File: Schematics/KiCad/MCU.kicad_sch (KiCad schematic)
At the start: 24 parts, among them J12 B5B-EH-A(LF)(SN), SW1 2-1977223-2, U10 STM32F446RET6, U16 LD1117S33CTR, Y1 ABLS-8.000MHZ-B2-T

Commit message: Fix all errors and warnings
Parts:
- removed C13, C2: 06035A300JAT2A, CAPC1608X90X35LL15T15, symbol Altium Content Vault:MCU_1_CAP_Altium Content Vault_0
- removed C14: GRM033R61A104KE15D, FP-GRM033-0_03-IPC_C, symbol Altium Content Vault:MCU_1_b4654b650e69147ec39a6b967a45e02_Altium Content Vault
- removed C15: 0805YD105MAT2A, CAPC2013X140X50NL20T25, symbol Altium Content Vault:MCU_1_CAP_Altium Content Vault_0
- removed C16, C18, C25, C26: GRM033R61A104KE15D, FP-GRM033-0_03-IPC_C, symbol Altium Content Vault:MCU_0_b4654b650e69147ec39a6b967a45e02_Altium Content Vault
- removed C17: CC0603KPX5R7BB225, FP-CC0603-DA-MFG, symbol Altium Content Vault:MCU_0_11868f565c42a9108669ba33697ecf6_Altium Content Vault
- removed C19: 1210ZC106KAT2A, FP-1210-L_3_3_0_4-W_2_5_0-IPC_A, symbol Altium Content Vault:MCU_2_b4654b650e69147ec39a6b967a45e02_Altium Content Vault
- removed C20: 1210ZC106KAT2A, FP-1210-L_3_3_0_4-W_2_5_0-IPC_A, symbol Altium Content Vault:MCU_0_b4654b650e69147ec39a6b967a45e02_Altium Content Vault
- removed C21: RM033R61A104KE15D, FP-GRM033-0_03-IPC_C, symbol Altium Content Vault:MCU_0_b4654b650e69147ec39a6b967a45e02_Altium Content Vault
- removed D1: APHCM2012SYCK-F01, FP-APHCM2012SYCK-F01-MFG, symbol Altium Content Vault:MCU_0_8706943c75ba83719d021d2fdc84c58_Altium Content Vault
- removed D2: APHD1608LZGCK, FP-APHD1608LZGCK-MFG, symbol Altium Content Vault:MCU_0_8706943c75ba83719d021d2fdc84c58_Altium Content Vault
- removed FB1: BLM03BB750SZ1D, FP-BLM03-0_03-d0_3-IPC_C, symbol Altium Content Vault:MCU_0_5f30dd21d616792df468990f7003faa_Altium Content Vault
- removed J12: B5B-EH-A(LF)(SN), FP-B5B-EH-A_LF_SN-MFG, symbol Altium Content Vault:MCU_0_bf93c07fd2649a848d0ec8585582aab_Altium Content Vault
- removed PS2: R-78E3.3-0.5, CONV_R-78E3.3-0.5, symbol R-78E3.3-0.5:MCU_0_R-78E3.3-0.5_R-78E3.3-0.5.IntLib
- removed R121: RQ73C1J100KBTD, FP-RQ731J-IPC_C, symbol Altium Content Vault:MCU_1_1029c3af85768c4190bb7ad29bc67b5_Altium Content Vault
- removed R122, R123: ERJH3GJ331V, FP-ERJH3G-MFG, symbol Altium Content Vault:MCU_0_1029c3af85768c4190bb7ad29bc67b5_Altium Content Vault
- removed SW1: 2-1977223-2, FP-2-1977223-2-MFG, symbol Altium Content Vault:MCU_0_b8895f3f4cefb76e1819d2863dba89b_Altium Content Vault
- removed U10: STM32F446RET6, STM-LQFP64_L, symbol Altium Content Vault:MCU_0_MC-ARM-STM32F446-LQFP64_Altium Content Vault
- removed U16: LD1117S33CTR, FP-SOT-223-0046067_14-MFG, symbol Altium Content Vault:MCU_0_7818869c5c16ceab15634627166a29d_Altium Content Vault
- removed Y1: ABLS-8.000MHZ-B2-T, FP-ABLS-MFG, symbol Altium Content Vault:MCU_1_c23a69dc6c9e2f18f2079038eb95dd1_Altium Content Vault
- added C12, C14, C15, C18, C19, C20, C23: 100n, Capacitor_SMD:C_0603_1608Metric, symbol Device:C
- added C16, C21: 1u, Capacitor_SMD:C_0603_1608Metric, symbol Device:C
- added C25, C26: 30pF, Capacitor_SMD:C_0603_1608Metric, symbol Device:C
- added C27: 2.2u, Capacitor_SMD:C_0603_1608Metric, symbol Device:C
- added D3, D4: LED, symbol Device:LED
- added FB2: 75, Resistor_SMD:R_0603_1608Metric, symbol Device:FerriteBead
- added J8: Conn_01x04_Pin, symbol Connector:Conn_01x04_Pin
- added R62, R63: 330, Resistor_SMD:R_0603_1608Metric, symbol Device:R_US
- added R64: 100k, Resistor_SMD:R_0603_1608Metric, symbol Device:R_US
- added U11: STM32F446RETx, Package_QFP:LQFP-64_10x10mm_P0.5mm, symbol MCU_ST_STM32F4:STM32F446RETx
- added Y1: ABLS-8.000MHZ-B2-T, symbol Device:Crystal
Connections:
- net GND: now also C12.2, C14.2, C15.2, C16.2, C18.2, C19.2, C20.2, C21.2, C23.2, C25.2, C26.2, C27.2, J8.1 (Pin_1), R64.2, U11.12 (VSSA), U11.18 (VSS), U11.31 (VSS), U11.47 (VSS), U11.63 (VSS)
- net MUX 0: now also U11.14 (PA0)
- net MUX 1: now also U11.15 (PA1)
- net MUX 2: now also U11.16 (PA2)
- net MUX 3: now also U11.17 (PA3)
- net MUX 4: now also U11.20 (PA4)
- net MUX 5: now also U11.21 (PA5)
- net MUX 6: now also U11.22 (PA6)
- net MUX 7: now also U11.23 (PA7)
- net MUX 8: now also U11.8 (PC0)
- net MUX 9: now also U11.9 (PC1)
- net S0: now also U11.55 (PB3)
- net S1: now also U11.57 (PB5)
- net S2: now also U11.56 (PB4)
- net S3: now also U11.29 (PB10)
- new net: C27.1, U11.30 (VCAP_1)
- new net: D3.2 (A), R62.2
- new net: D3.1 (K), U11.39 (PC8)
- new net: D4.1 (K), U11.40 (PC9)
- new net: D4.2 (A), R63.2
- new net: C25.1, U11.5 (PH0), Y1.1
- new net: C26.1, U11.6 (PH1), Y1.2
- new net +3.3VA: C15.1, C16.1, FB2.2, U11.13 (VDDA)
- new net +3V3: C12.1, C18.1, C19.1, C20.1, C21.1, C23.1, FB2.1, J8.4 (Pin_4), R62.1, R63.1, U11.1 (VBAT), U11.19 (VDD), U11.32 (VDD), U11.48 (VDD), U11.64 (VDD)
- new net BOOT0: R64.1, U11.60 (BOOT0)
- new net CAN RX: U11.45 (PA12)
- new net CAN TX: U11.44 (PA11)
- new net Fault Line 1: U11.41 (PA8)
- new net NRST: C14.1, U11.7 (NRST)
- new net SWCLK: J8.2 (Pin_2), U11.49 (PA14)
- new net SWDIO: J8.3 (Pin_3), U11.46 (PA13)
- no-connect marks 28 -> 27
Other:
- note removed: "STLINK"

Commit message: Update schematics
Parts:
- D3, D4: footprint (none) -> LED_SMD:LED_0603_1608Metric
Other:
- moved on the sheet: D3, D4, R62, R63
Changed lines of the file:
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@@
+	(wire
+		(pts
+			(xy 143.51 132.08) (xy 142.24 132.08)
+		)
+		(stroke
+			(width 0)
+			(type default)
+		)
+	)
 	(wire
 		(pts
@@
 	(wire
 		(pts
+			(xy 143.51 135.89) (xy 142.24 135.89)
+		)
+		(stroke
+			(width 0)
+			(type default)
+		)
+	)
+	(wire
+		(pts
 			(xy 232.41 125.73) (xy 308.61 125.73)
 		)
@@
 	(wire
 		(pts
-			(xy 148.59 135.89) (xy 191.77 135.89)
+			(xy 151.13 135.89) (xy 191.77 135.89)
 		)
 		(stroke
@@
 	(wire
 		(pts
-			(xy 148.59 132.08) (xy 152.4 132.08)
+			(xy 151.13 132.08) (xy 152.4 132.08)
 		)
 		(stroke
@@
 	(wire
 		(pts
-			(xy 133.35 132.08) (xy 130.81 132.08)
+			(xy 134.62 132.08) (xy 130.81 132.08)
 		)
 		(stroke
@@
 	(wire
 		(pts
-			(xy 133.35 135.89) (xy 130.81 135.89)
+			(xy 134.62 135.89) (xy 130.81 135.89)
 		)
 		(stroke
@@
 	(symbol
 		(lib_id "Device:R_US")
-		(at 137.16 132.08 90)
+		(at 138.43 132.08 90)
 		(unit 1)
 		(exclude_from_sim no)
@@
 		(dnp no)
 		(property "Reference" "R62"
-			(at 132.842 130.81 90)
+			(at 134.112 130.81 90)
 			(effects
 				(font
@@
 		)
 		(property "Value" "330"
-			(at 140.97 131.064 90)
+			(at 142.24 131.064 90)
 			(effects
 				(font
@@
 		)
 		(property "Footprint" "Resistor_SMD:R_0603_1608Metric"
-			(at 137.414 131.064 90)
+			(at 138.684 131.064 90)
 			(effects
 				(font
@@
 		)
 		(property "Datasheet" "~"
-			(at 137.16 132.08 0)
+			(at 138.43 132.08 0)
 			(effects
 				(font
@@
 		)
 		(property "Description" "Resistor, US symbol"
-			(at 137.16 132.08 0)
+			(at 138.43 132.08 0)
 			(effects
 				(font
@@
 	(symbol
 		(lib_id "Device:LED")
-		(at 144.78 132.08 180)
+		(at 147.32 132.08 180)
 		(unit 1)
 		(exclude_from_sim no)
@@
 		(dnp no)
 		(property "Reference" "D3"
-			(at 150.876 130.556 0)
+			(at 153.416 130.556 0)
 			(effects
 				(font
@@
 		)
 		(property "Value" "LED"
-			(at 154.686 130.302 0)
-			(effects
-				(font
-					(size 1.27 1.27)
-				)
-			)
-		)
-		(property "Footprint" ""
-			(at 144.78 132.08 0)
+			(at 157.226 130.302 0)
+			(effects
+				(font
+					(size 1.27 1.27)
+				)
+			)
+		)
+		(property "Footprint" "LED_SMD:LED_0603_1608Metric"
+			(at 147.32 132.08 0)
 			(effects
 				(font
@@
 		)
 		(property "Datasheet" "~"
-			(at 144.78 132.08 0)
+			(at 147.32 132.08 0)
 			(effects
 				(font
@@
 		)
 		(property "Description" "Light emitting diode"
-			(at 144.78 132.08 0)
+			(at 147.32 132.08 0)
 			(effects
 				(font
@@
 		)
 		(property "Sim.Pins" "1=K 2=A"
-			(at 144.78 132.08 0)
+			(at 147.32 132.08 0)
+			(effects
+				(font
+					(size 1.27 1.27)
+				)
+				(hide yes)
+			)
+		)
+		(property "MPN" ""
+			(at 147.32 132.08 0)
+			(effects
+				(font
+					(size 1.27 1.27)
+				)
+				(hide yes)
+			)
+		)
+		(property "JLCPCB Part #" ""
+			(at 147.32 132.08 0)
 			(effects
 				(font
@@
 	(symbol
 		(lib_id "Device:LED")
-		(at 144.78 135.89 180)
+		(at 147.32 135.89 180)
 		(unit 1)
 		(exclude_from_sim no)
@@
 		(dnp no)
 		(property "Reference" "D4"
-			(at 150.622 137.16 0)
+			(at 153.162 137.16 0)
 			(effects
 				(font
@@
 		)
 		(property "Value" "LED"
-			(at 154.432 137.16 0)
-			(effects
-				(font
-					(size 1.27 1.27)
-				)
-			)
-		)
-		(property "Footprint" ""
-			(at 144.78 135.89 0)
+			(at 156.972 137.16 0)
+			(effects
+				(font
+					(size 1.27 1.27)
+				)
+			)
+		)
+		(property "Footprint" "LED_SMD:LED_0603_1608Metric"
+			(at 147.32 135.89 0)
 			(effects
 				(font
@@
 		)
 		(property "Datasheet" "~"
-			(at 144.78 135.89 0)
+			(at 147.32 135.89 0)
 			(effects
 				(font
@@
 		)
 		(property "Description" "Light emitting diode"
-			(at 144.78 135.89 0)
+			(at 147.32 135.89 0)
 			(effects
 				(font
@@
 		)
 		(property "Sim.Pins" "1=K 2=A"
-			(at 144.78 135.89 0)
+			(at 147.32 135.89 0)
+			(effects
+				(font
+					(size 1.27 1.27)
+				)
+				(hide yes)
+			)
+		)
+		(property "MPN" ""
+			(at 147.32 135.89 0)
+			(effects
+				(font
+					(size 1.27 1.27)
+				)
+				(hide yes)
+			)
+		)
+		(property "JLCPCB Part #" ""
+			(at 147.32 135.89 0)
 			(effects
 				(font
@@
 	(symbol
 		(lib_id "Device:R_US")
-		(at 137.16 135.89 90)
+		(at 138.43 135.89 90)
 		(unit 1)
 		(exclude_from_sim no)
@@
 		(dnp no)
 		(property "Reference" "R63"
-			(at 132.842 134.62 90)
+			(at 134.112 134.62 90)
 			(effects
 				(font
@@
 		)
 		(property "Value" "330"
-			(at 140.97 134.874 90)
+			(at 142.24 134.874 90)
 			(effects
 				(font
@@
 		)
 		(property "Footprint" "Resistor_SMD:R_0603_1608Metric"
-			(at 137.414 134.874 90)
+			(at 138.684 134.874 90)
 			(effects
 				(font
@@
 		)
 		(property "Datasheet" "~"
-			(at 137.16 135.89 0)
+			(at 138.43 135.89 0)
 			(effects
 				(font
@@
 		)
 		(property "Description" "Resistor, US symbol"
-			(at 137.16 135.89 0)
-			(effects
-				(font
+			(at 138.43 135.89 0)
+			(effects
+				(font

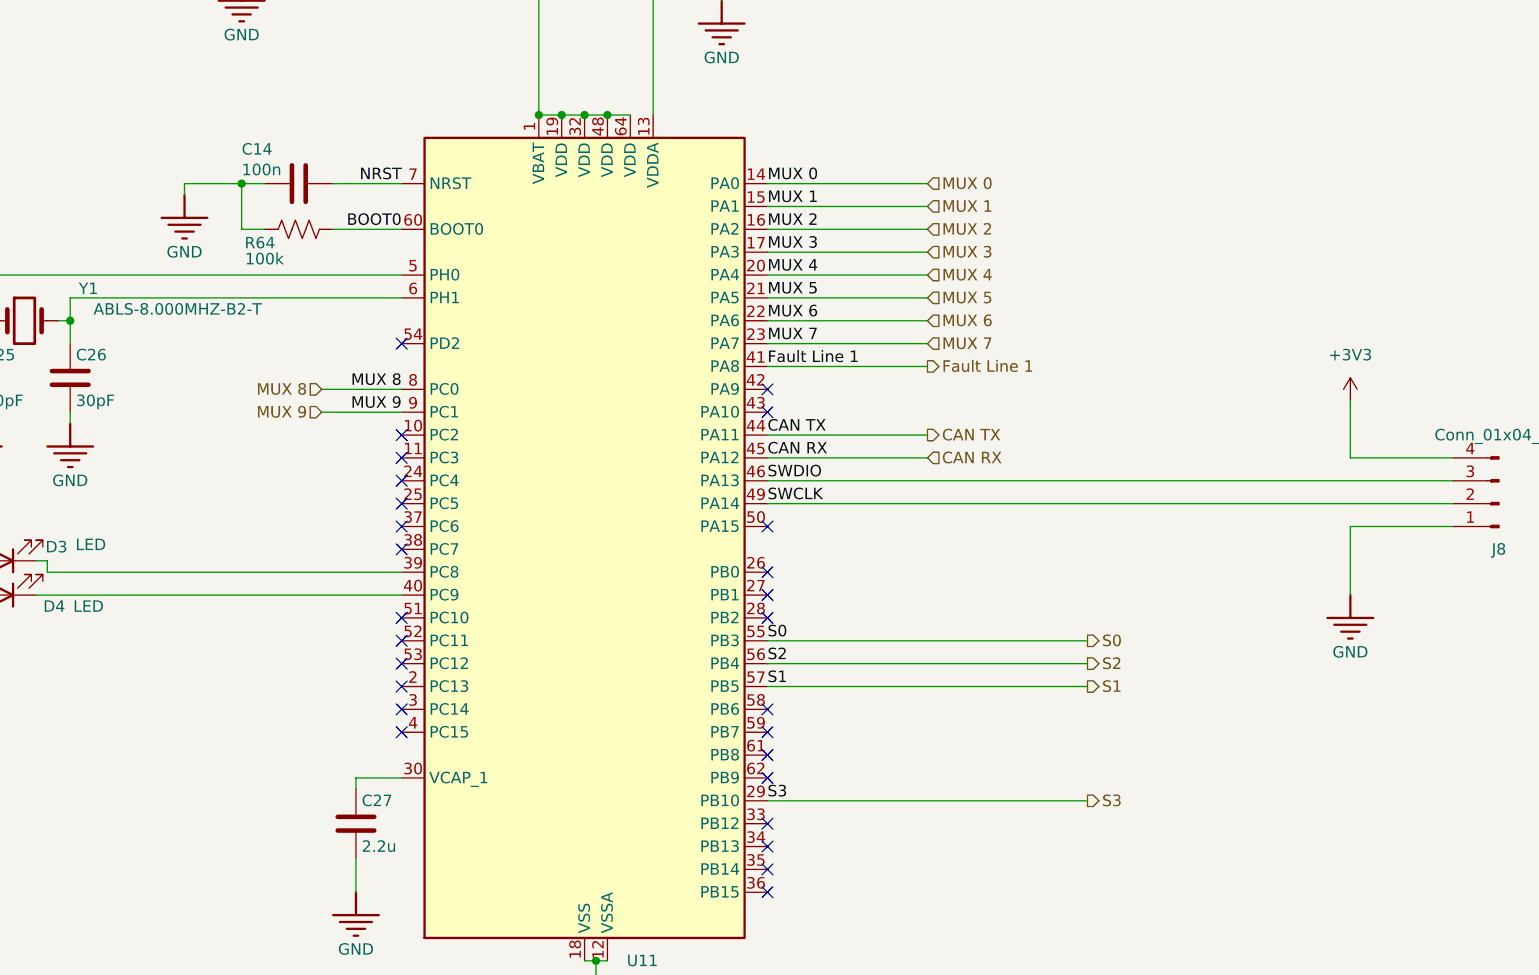
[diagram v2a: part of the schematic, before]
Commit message: Condense layout to 2 layers
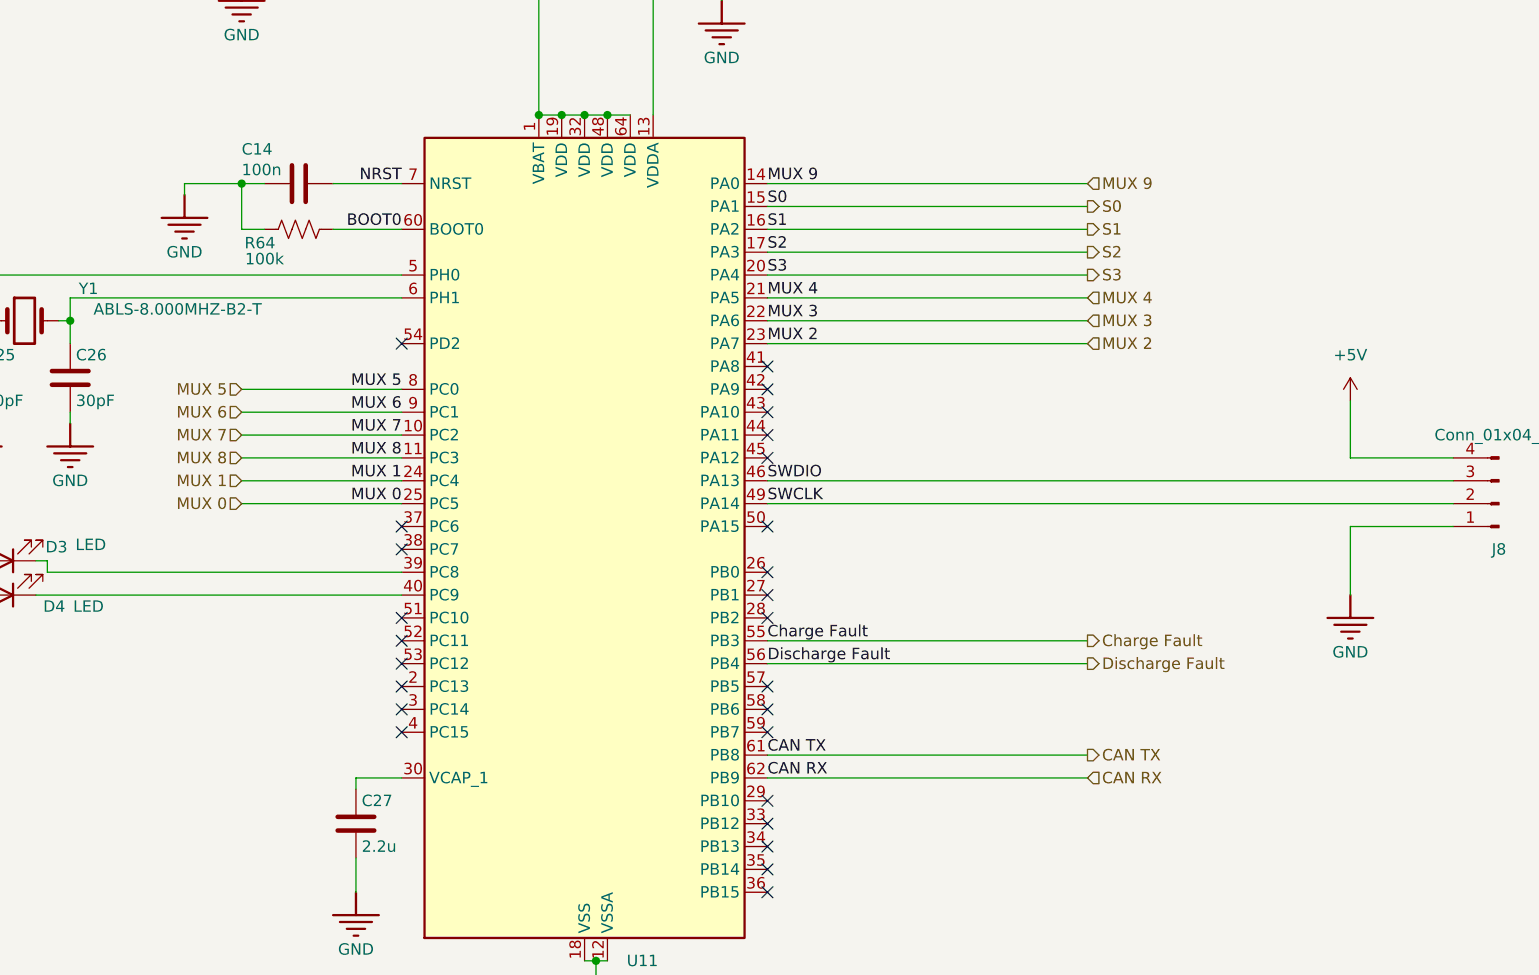
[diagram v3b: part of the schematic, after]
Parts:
- J8: footprint (none) -> Connector_PinHeader_2.54mm:PinHeader_1x04_P2.54mm_Vertical
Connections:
- net +3V3: no longer J8.4 (Pin_4)
- net CAN RX: now also U11.62 (PB9); no longer U11.45 (PA12)
- net CAN TX: now also U11.61 (PB8); no longer U11.44 (PA11)
- net MUX 0: now also U11.25 (PC5); no longer U11.14 (PA0)
- net MUX 1: now also U11.24 (PC4); no longer U11.15 (PA1)
- net MUX 2: now also U11.23 (PA7); no longer U11.16 (PA2)
- net MUX 3: now also U11.22 (PA6); no longer U11.17 (PA3)
- net MUX 4: now also U11.21 (PA5); no longer U11.20 (PA4)
- net MUX 5: now also U11.8 (PC0); no longer U11.21 (PA5)
- net MUX 6: now also U11.9 (PC1); no longer U11.22 (PA6)
- net MUX 7: now also U11.10 (PC2); no longer U11.23 (PA7)
- net MUX 8: now also U11.11 (PC3); no longer U11.8 (PC0)
- net MUX 9: now also U11.14 (PA0); no longer U11.9 (PC1)
- net S0: now also U11.15 (PA1); no longer U11.55 (PB3)
- net S1: now also U11.16 (PA2); no longer U11.57 (PB5)
- net S2: now also U11.17 (PA3); no longer U11.56 (PB4)
- net S3: now also U11.20 (PA4); no longer U11.29 (PB10)
- net Fault Line 1: no longer names the net of U11.41 (PA8)
- new net +5V: J8.4 (Pin_4)
- new net Charge Fault: U11.55 (PB3)
- new net Discharge Fault: U11.56 (PB4)
- no-connect marks 27 -> 26

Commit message: More pcb layout work
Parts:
- removed C25, C26: 30pF, Capacitor_SMD:C_0603_1608Metric, symbol Device:C
- removed Y1: ABLS-8.000MHZ-B2-T, symbol Device:Crystal
- added C30, C31: 6pF, Capacitor_SMD:C_0402_1005Metric, symbol Device:C
- added Y2: 7B008000F01, Crystal:Crystal_SMD_3225-4Pin_3.2x2.5mm, symbol Device:Crystal_GND24
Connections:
- net GND: now also C30.2, C31.2, Y2.2, Y2.4
- net at U11.5 (PH0): now also C30.1, Y2.3
- net at U11.6 (PH1): now also C31.1, Y2.1
